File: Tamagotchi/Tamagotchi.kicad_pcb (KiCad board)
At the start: 2 copper layers, 6 parts, among them SW1 SW_Push, SW2 SW_Push, SW3 SW_Push

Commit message: commiting this for now cuz my kicad is tweaking
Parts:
- added R1: R, Resistor_THT:R_Axial_DIN0204_L3.6mm_D1.6mm_P5.08mm_Horizontal, F.Cu at (223.0, 78.0)
- added R2: R, Resistor_THT:R_Axial_DIN0204_L3.6mm_D1.6mm_P5.08mm_Horizontal, F.Cu at (244.9, 74.0)
- added R3: R, Resistor_THT:R_Axial_DIN0204_L3.6mm_D1.6mm_P5.08mm_Horizontal, F.Cu at (264.9, 78.5)
- added U1: XIAO-ESP32-C6-DIP, Seeed Studio XIAO Series Library:XIAO-ESP32-C6-DIP, F.Cu at (247.1, 119.1)
- added U2: DM-OLED096-636, DM-OLED096-636 (1):MODULE_DM-OLED096-636, F.Cu at (246.5, 93.5)
- moved SW3 276.2 mm to (265.5, 126.7)
- moved SW2 270.5 mm to (246.0, 134.2)
- moved D3 259.1 mm to (265.7, 70.8)
- moved SW1 255.8 mm to (224.5, 126.7)
- moved D2 245.0 mm to (246.2, 66.6)
- moved D1 230.2 mm to (224.2, 69.8)
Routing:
- net GND: track 0.00 -> 163.2 mm
- net Net-(U1-GPIO21_D3): track 0.00 -> 52.2 mm
- net +3V3: track 0.00 -> 42.0 mm
- net Net-(U1-GPIO22_D4_SDA): track 0.00 -> 40.1 mm
- net Net-(U1-GPIO17_D7_RX): track 0.00 -> 39.7 mm
- net Net-(U1-GPIO16_D6_TX): track 0.00 -> 39.0 mm
- net Net-(U1-GPIO23_D5_SCL): track 0.00 -> 34.9 mm
- net Net-(U1-GPIO2_A2_D2): track 0.00 -> 17.9 mm
- net Net-(U1-GPIO1_A1_D1): track 0.00 -> 11.5 mm
- net Net-(D1-A): track 0.00 -> 9.75 mm
- net Net-(D3-A): track 0.00 -> 9.07 mm
- net Net-(D2-A): track 0.00 -> 7.88 mm
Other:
- board outline added: 84.6 x 124 mm

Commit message: did my pcb I guess some slik screen errors idk how to fix rn
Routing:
- net Net-(U1-GPIO0_A0_D0): track 0.00 -> 26.1 mm

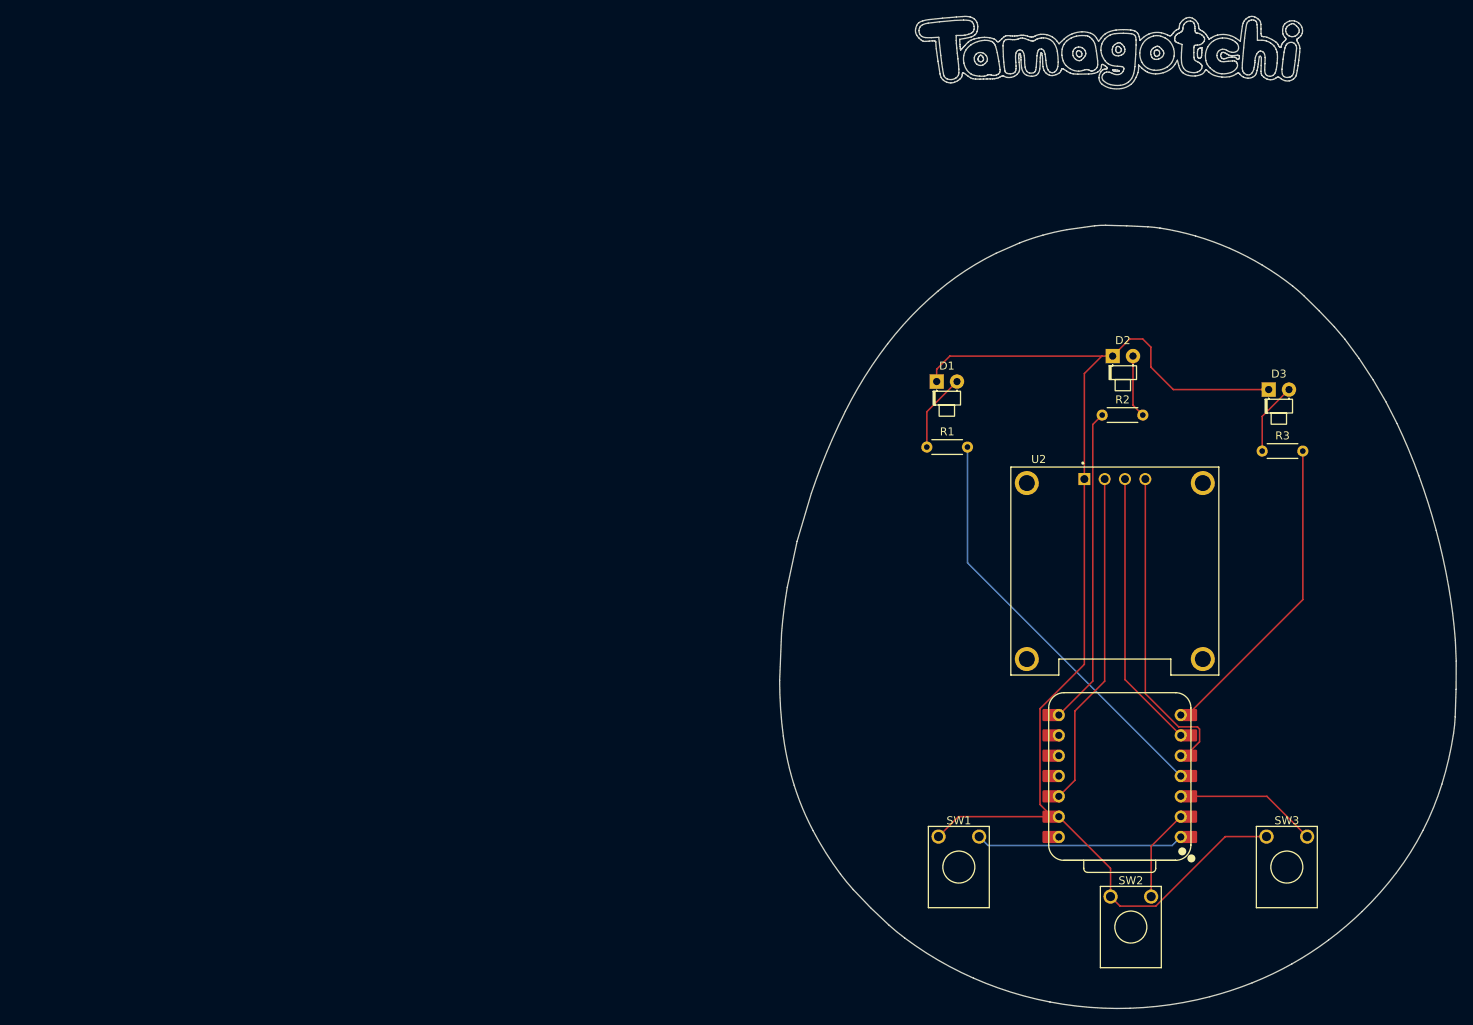
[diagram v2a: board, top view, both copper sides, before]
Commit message: added some resistor and capacitors
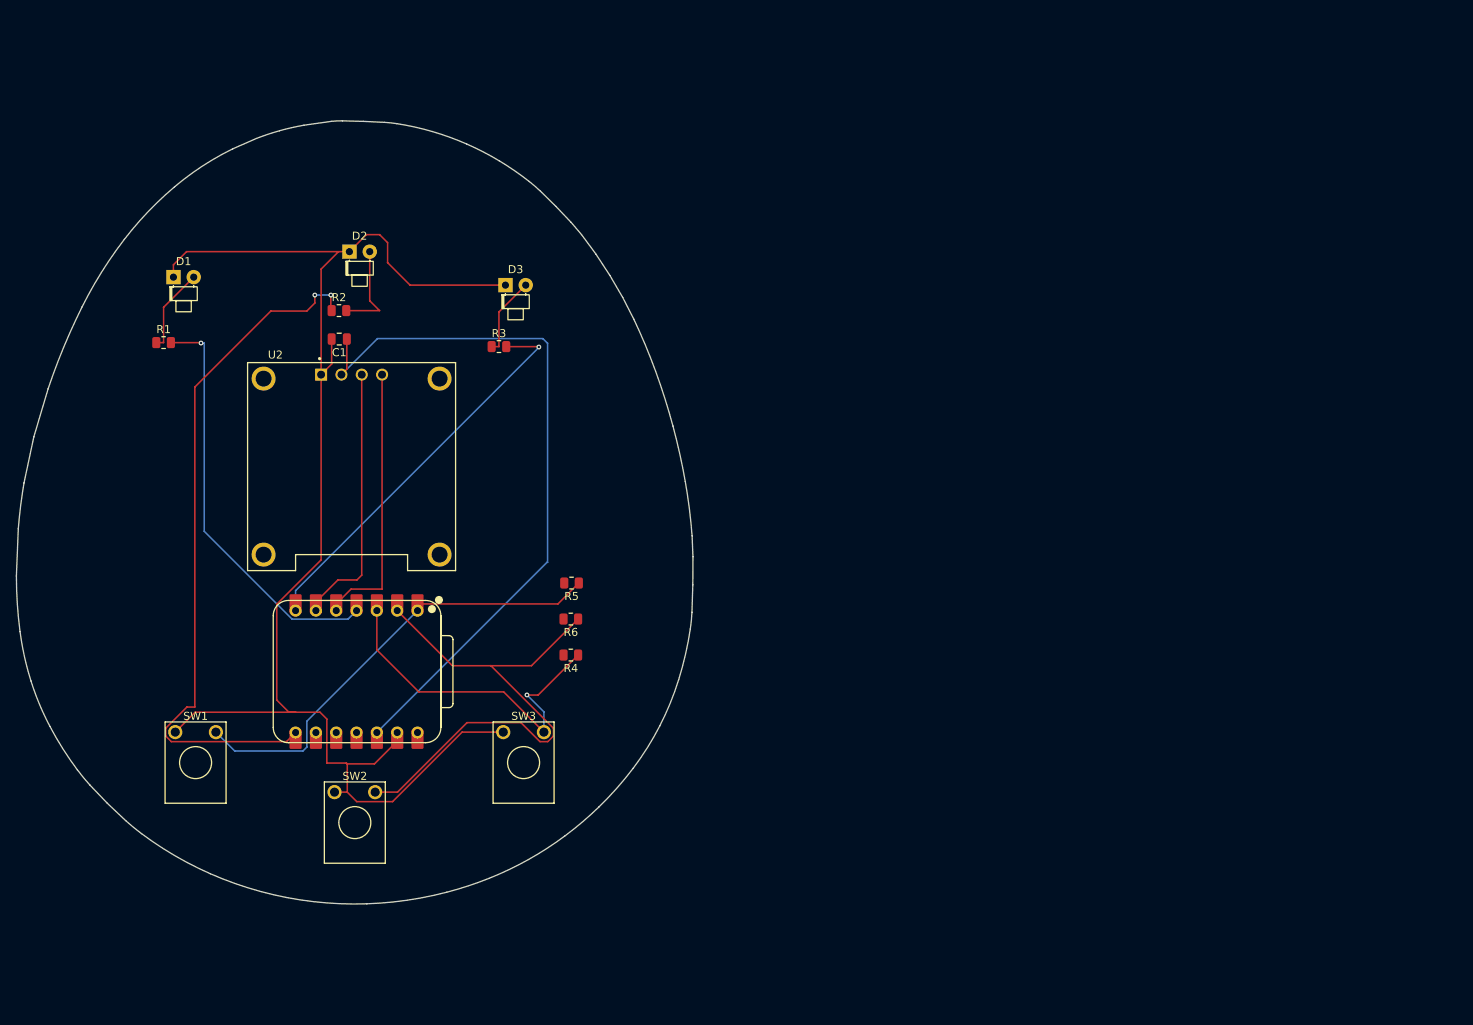
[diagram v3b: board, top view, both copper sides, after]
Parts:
- added C1: C, Capacitor_SMD:C_0805_2012Metric, F.Cu at (149.6, 64.5)
- added R4: 10k, Resistor_SMD:R_0805_2012Metric, F.Cu at (178.5, 104.0)
- added R5: 10K, Resistor_SMD:R_0805_2012Metric, F.Cu at (178.6, 95.0)
- added R6: 10k, Resistor_SMD:R_0805_2012Metric, F.Cu at (178.5, 99.5)
- R1, R2, R3: value R -> 1K; footprint Resistor_THT:R_Axial_DIN0204_L3.6mm_D1.6mm_P5.08mm_Horizontal -> Resistor_SMD:R_0805_2012Metric
- moved SW2 97.9 mm to (149.0, 121.1)
- moved D3 96.3 mm to (170.3, 57.8)
- moved R3 96.3 mm to (169.5, 65.4)
- moved SW1 96.3 mm to (129.1, 113.6)
- moved U1 96.3 mm to (151.7, 106.1), turned to 0 degrees
- moved R1 96.3 mm to (127.6, 64.9)
- moved D1 96.3 mm to (128.8, 56.8)
- moved D2 96.3 mm to (150.8, 53.6)
- moved R2 96.3 mm to (149.5, 60.9)
- moved SW3 96.3 mm to (170.1, 113.6)
- moved U2 96.3 mm to (151.1, 80.4)
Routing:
- net Net-(U1-GPIO1_A1_D1): track 11.5 -> 67.1 mm
- net +3V3: track 42.0 -> 90.1 mm
- net Net-(U1-GPIO17_D7_RX): track 39.7 -> 87.0 mm, vias 0 -> 2
- net Net-(U1-GPIO0_A0_D0): track 26.1 -> 56.6 mm
- net Net-(U1-GPIO2_A2_D2): track 17.9 -> 44.1 mm, vias 0 -> 1
- net GND: track 163.2 -> 181.6 mm
- net Net-(U1-GPIO16_D6_TX): track 39.0 -> 49.8 mm, vias 0 -> 1
- net Net-(U1-GPIO22_D4_SDA): track 40.1 -> 34.1 mm
- net Net-(D2-A): track 7.88 -> 12.0 mm
- net Net-(U1-GPIO23_D5_SCL): track 34.9 -> 33.3 mm
- net Net-(D3-A): track 9.07 -> 9.99 mm
- net Net-(D1-A): track 9.75 -> 10.7 mm
- net Net-(U1-GPIO21_D3): track 52.2 -> 51.7 mm, vias 0 -> 1
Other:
- board size 84.6 x 124 mm -> 84.6 x 97.9 mm

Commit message: Done pcb!!!
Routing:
- net +3V3: track 90.1 -> 102.9 mm, vias 0 -> 1
- net GND: track 181.6 -> 194.0 mm
- net Net-(U1-GPIO17_D7_RX): track 87.0 -> 78.2 mm
- net Net-(U1-GPIO21_D3): track 51.7 -> 59.6 mm
- net Net-(U1-GPIO1_A1_D1): track 67.1 -> 72.5 mm
- net Net-(D2-A): track 12.0 -> 9.59 mm
- net Net-(U1-GPIO2_A2_D2): track 44.1 -> 42.0 mm
- net Net-(U1-GPIO16_D6_TX): track 49.8 -> 50.9 mm
- net Net-(D1-A): track 10.7 -> 11.6 mm
- added copper zone on B.Cu, net GND
- added copper zone on F.Cu, net GND

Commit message: trying to do final checks on everything as well as finishing writing the readme
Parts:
- C1: value C -> 0.1uF
- D1, D2, D3: footprint LED_THT:LED_D1.8mm_W1.8mm_H2.4mm_Horizontal_O1.27mm_Z4.9mm -> LED_THT:LED_D1.8mm_W1.8mm_H2.4mm_Horizontal_O1.27mm_Z1.6mm

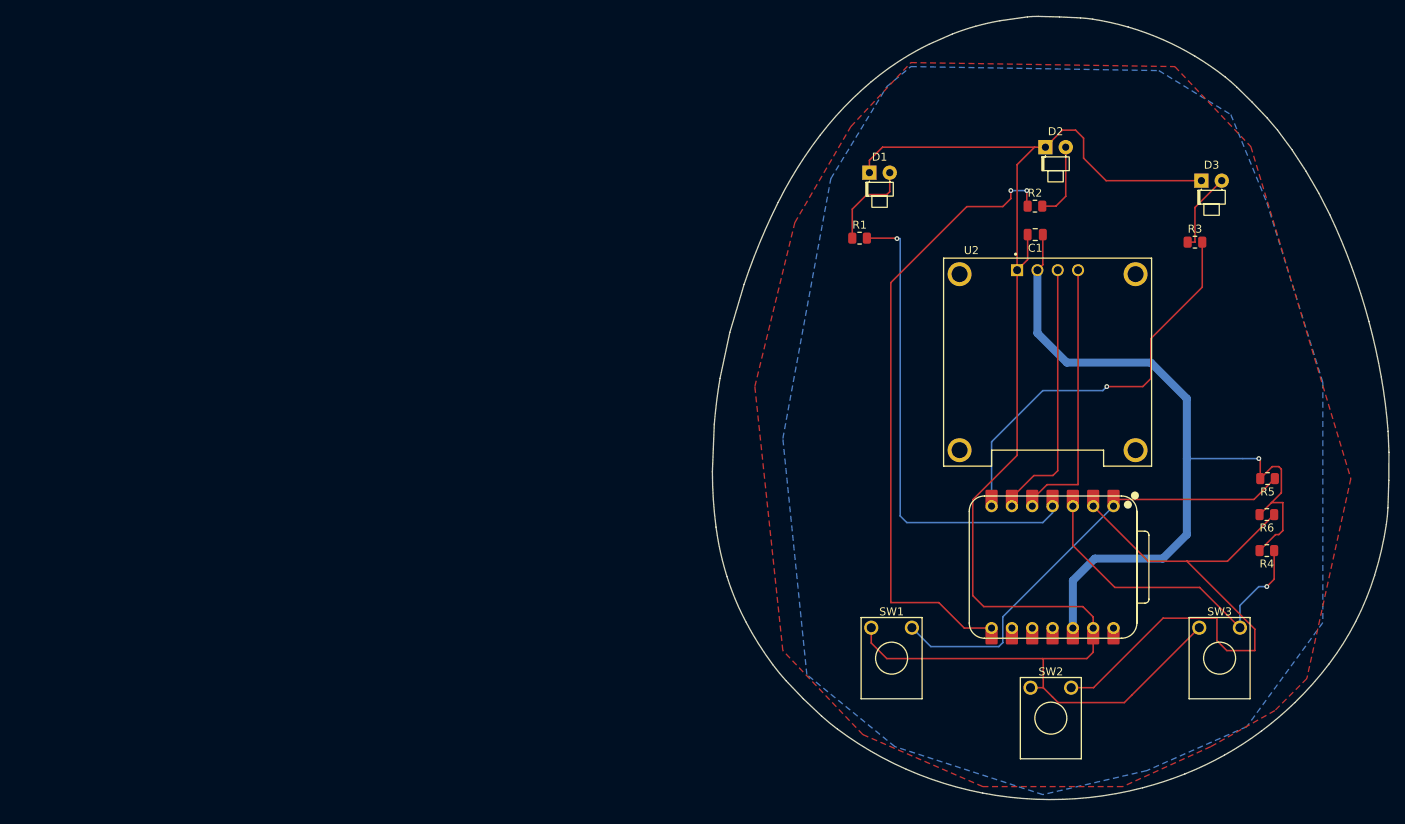
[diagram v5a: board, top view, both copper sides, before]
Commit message: had to rewire pcb due to changing the esp32
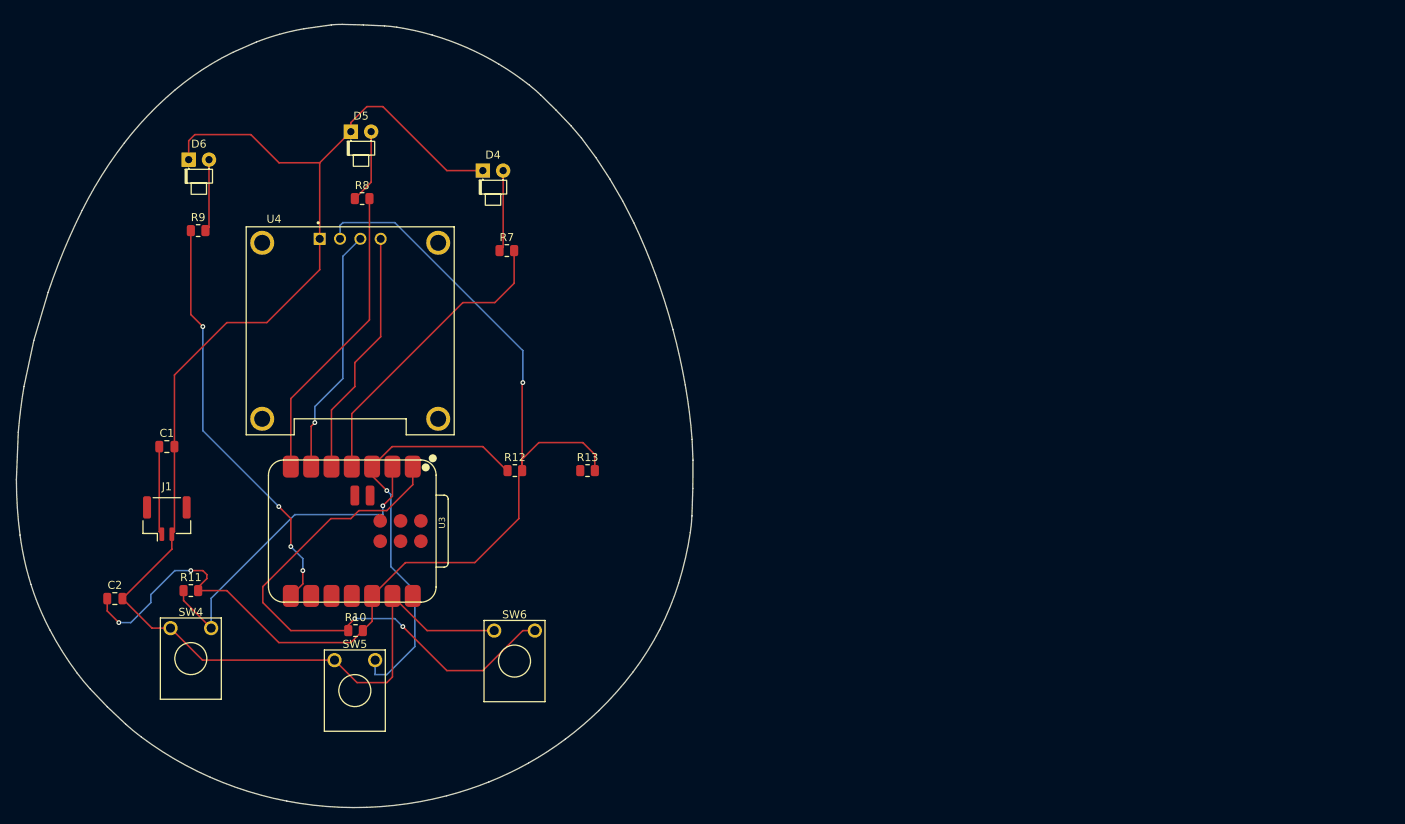
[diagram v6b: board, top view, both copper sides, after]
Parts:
- removed D1, D2, D3: LED, LED_THT:LED_D1.8mm_W1.8mm_H2.4mm_Horizontal_O1.27mm_Z1.6mm
- removed R1, R2, R3: 1K, Resistor_SMD:R_0805_2012Metric
- removed R4, R6: 10k, Resistor_SMD:R_0805_2012Metric
- removed R5: 10K, Resistor_SMD:R_0805_2012Metric
- removed SW1, SW2, SW3: SW_Push, Button_Switch_THT:KSA_Tactile_SPST
- removed U1: XIAO-ESP32-C6-DIP, Seeed Studio XIAO Series Library:XIAO-ESP32-C6-DIP
- removed U2: DM-OLED096-636, DM-OLED096-636 (1):MODULE_DM-OLED096-636
- added C2: 0.1uF, Capacitor_SMD:C_0805_2012Metric, F.Cu at (34.5, 110.0)
- added D4: LED, LED_THT:LED_D1.8mm_W1.8mm_H2.4mm_Horizontal_O1.27mm_Z1.6mm, F.Cu at (80.5, 56.5)
- added D5: LED, LED_THT:LED_D1.8mm_W1.8mm_H2.4mm_Horizontal_O1.27mm_Z1.6mm, F.Cu at (64.0, 51.6)
- added D6: LED, LED_THT:LED_D1.8mm_W1.8mm_H2.4mm_Horizontal_O1.27mm_Z1.6mm, F.Cu at (43.7, 55.1)
- added J1: Battery connector, Connector_JST:JST_GH_BM02B-GHS-TBT_1x02-1MP_P1.25mm_Vertical, F.Cu at (41.0, 100.0)
- added R10: 10K, Resistor_SMD:R_0805_2012Metric, F.Cu at (64.6, 114.0)
- added R11: 10k, Resistor_SMD:R_0805_2012Metric, F.Cu at (44.0, 109.0)
- added R12: 10k, Resistor_SMD:R_0805_2012Metric, F.Cu at (84.5, 94.0)
- added R13: 10k, Resistor_SMD:R_0805_2012Metric, F.Cu at (93.6, 94.0)
- added R7: 1K, Resistor_SMD:R_0805_2012Metric, F.Cu at (83.5, 66.5)
- added R8: 1K, Resistor_SMD:R_0805_2012Metric, F.Cu at (65.4, 60.0)
- added R9: 1K, Resistor_SMD:R_0805_2012Metric, F.Cu at (44.9, 64.0)
- added SW4: SW_Push, Button_Switch_THT:KSA_Tactile_SPST, F.Cu at (41.5, 113.7)
- added SW5: SW_Push, Button_Switch_THT:KSA_Tactile_SPST, F.Cu at (62.0, 117.7)
- added SW6: SW_Push, Button_Switch_THT:KSA_Tactile_SPST, F.Cu at (81.9, 114.0)
- added U3: XIAO-ESP32-C3-SMD, Seeed Studio XIAO Series Library:XIAO-ESP32-C3-SMD, F.Cu at (53.6, 92.7)
- added U4: DM-OLED096-636, DM-OLED096-636 (1):MODULE_DM-OLED096-636, F.Cu at (63.9, 76.5)
- C1: value 0.1uF -> C_Polarized
- moved C1 111.7 mm to (41.0, 91.0), turned to 0 degrees
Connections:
- C1 pad 1: +3V3 -> Net-(J1-Pin_1)
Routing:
- net Net-(U1-GPIO17_D7_RX): track 78.2 -> 0.00 mm, vias 2 -> 0
- net Net-(U1-GPIO1_A1_D1): track 72.5 -> 0.00 mm
- net Net-(U3-GPIO2_A0_D0): track 0.00 -> 69.5 mm, vias 0 -> 2
- net Net-(U1-GPIO21_D3): track 59.6 -> 0.00 mm, vias 1 -> 0
- net Net-(U1-GPIO0_A0_D0): track 56.6 -> 0.00 mm
- net Net-(U3-GPIO4_A2_D2): track 0.00 -> 52.2 mm, vias 0 -> 1
- net Net-(U3-GPIO20_D7_RX): track 0.00 -> 52.1 mm, vias 0 -> 4
- net Net-(U1-GPIO16_D6_TX): track 50.9 -> 0.00 mm, vias 1 -> 0
- net Net-(U3-GPIO3_A1_D1): track 0.00 -> 42.1 mm, vias 0 -> 1
- net Net-(U1-GPIO2_A2_D2): track 42.0 -> 0.00 mm, vias 1 -> 0
- net Net-(U3-GPIO5_A3_D3): track 0.00 -> 37.8 mm
- net Net-(U3-GPIO21_D6_TX): track 0.00 -> 37.6 mm
- net +3V3: track 102.9 -> 138.1 mm, vias 1 -> 3
- net Net-(U1-GPIO22_D4_SDA): track 34.1 -> 0.00 mm
- net Net-(U1-GPIO23_D5_SCL): track 33.3 -> 0.00 mm
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- removed copper zone on B.Cu, net GND
- removed copper zone on F.Cu, net GND

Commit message: have so much to fixxx
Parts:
- added BT1: Battery_Cell, Battery:BatteryHolder_Keystone_3034_1x20mm, F.Cu at (36.9, 78.5)
- added REF**: MountingHole_3mm, MountingHole:MountingHole_3mm, F.Cu at (93.0, 62.5)
- added REF**: MountingHole_2.1mm, MountingHole:MountingHole_2.1mm, F.Cu at (53.0, 65.5)
- added REF**: MountingHole_3mm, MountingHole:MountingHole_3mm, F.Cu at (37.5, 62.5)
- added REF**: MountingHole_2.1mm, MountingHole:MountingHole_2.1mm, F.Cu at (75.0, 65.5)
- added REF**: MountingHole_3mm, MountingHole:MountingHole_3mm, F.Cu at (52.5, 128.0)
- added REF**: MountingHole_2.1mm, MountingHole:MountingHole_2.1mm, F.Cu at (75.0, 87.5)
- added REF**: MountingHole_2.1mm, MountingHole:MountingHole_2.1mm, F.Cu at (53.0, 87.5)
- added REF**: MountingHole_3mm, MountingHole:MountingHole_3mm, F.Cu at (77.0, 127.5)
- SW4, SW5, SW6: footprint Button_Switch_THT:KSA_Tactile_SPST -> Button_Switch_THT:SW_PUSH_6mm_H5mm
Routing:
- net Net-(BT1-+): track 0.00 -> 40.7 mm, vias 0 -> 2
- net GND: track 178.4 -> 190.8 mm
- net Net-(U3-GPIO3_A1_D1): track 42.1 -> 53.5 mm, vias 1 -> 3
- net Net-(U3-GPIO4_A2_D2): track 52.2 -> 59.3 mm
- net Net-(U3-GPIO2_A0_D0): track 69.5 -> 74.5 mm

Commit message: just saving some things last min
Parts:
- removed BT1: Battery_Cell, Battery:BatteryHolder_Keystone_3034_1x20mm
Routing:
- net Net-(BT1-+): track 40.7 -> 0.00 mm, vias 2 -> 0
